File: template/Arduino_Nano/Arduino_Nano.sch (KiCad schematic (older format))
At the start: 6 parts, among them P1 Digital, P2 Analog, P3 CONN_1, P4 CONN_1, P5 CONN_1, P6 CONN_1

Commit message: add board Micro
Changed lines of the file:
@@
 L +3.3V #PWR3
 U 1 1 551D9E93
-P 11000 2575
-F 0 "#PWR3" H 11000 2535 30  0001 C CNN
-F 1 "+3.3V" H 11000 2685 30  0000 C CNN
-F 2 "" H 11000 2575 60  0000 C CNN
-F 3 "" H 11000 2575 60  0000 C CNN
-	1    11000 2575
+P 11125 2575
+F 0 "#PWR3" H 11125 2535 30  0001 C CNN
+F 1 "+3.3V" H 11125 2685 30  0000 C CNN
+F 2 "" H 11125 2575 60  0000 C CNN
+F 3 "" H 11125 2575 60  0000 C CNN
+	1    11125 2575
 	1    0    0    -1
 $EndComp
@@
 L +5V #PWR2
 U 1 1 551D9FBD
-P 11000 1575
-F 0 "#PWR2" H 11000 1665 20  0001 C CNN
-F 1 "+5V" H 11000 1665 30  0000 C CNN
-F 2 "" H 11000 1575 60  0000 C CNN
-F 3 "" H 11000 1575 60  0000 C CNN
-	1    11000 1575
+P 11125 1575
+F 0 "#PWR2" H 11125 1665 20  0001 C CNN
+F 1 "+5V" H 11125 1665 30  0000 C CNN
+F 2 "" H 11125 1575 60  0000 C CNN
+F 3 "" H 11125 1575 60  0000 C CNN
+	1    11125 1575
 	1    0    0    -1
 $EndComp
@@
 L GND #PWR4
 U 1 1 551D9FD7
-P 11125 1475
-F 0 "#PWR4" H 11125 1475 30  0001 C CNN
-F 1 "GND" H 11125 1405 30  0001 C CNN
-F 2 "" H 11125 1475 60  0000 C CNN
-F 3 "" H 11125 1475 60  0000 C CNN
-	1    11125 1475
+P 11000 1475
+F 0 "#PWR4" H 11000 1475 30  0001 C CNN
+F 1 "GND" H 11000 1405 30  0001 C CNN
+F 2 "" H 11000 1475 60  0000 C CNN
+F 3 "" H 11000 1475 60  0000 C CNN
+	1    11000 1475
 	1    0    0    -1
 $EndComp
@@
 	11225 2850 8600 2850
 Wire Wire Line
-	11000 1600 11000 1575
-Wire Wire Line
-	11125 1400 11125 1475
-Wire Wire Line
-	11000 2600 11000 2575
-Wire Wire Line
 	8750 1600 8750 1675
 Wire Wire Line
 	10500 2700 10875 2700
 Wire Wire Line
-	10500 2600 11000 2600
+	10500 2600 11125 2600
 Wire Wire Line
 	10500 2500 10875 2500
@@
 	10500 1700 10875 1700
 Wire Wire Line
-	10500 1600 11000 1600
+	10500 1600 11125 1600
 Wire Wire Line
 	10500 1500 10875 1500
-Wire Wire Line
-	10500 1400 11125 1400
 Wire Wire Line
 	10500 1300 10875 1300
@@
 Wire Wire Line
 	8875 1300 9425 1300
+Wire Wire Line
+	11125 1600 11125 1575
+Wire Wire Line
+	11000 1475 11000 1400
+Wire Wire Line
+	11000 1400 10500 1400
+Wire Wire Line
+	11125 2600 11125 2575
 $EndSCHEMATC

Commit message: Correction schématics
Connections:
- wire segments 34 -> 35
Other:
- moved on the sheet: P1, P2, P3, P4, P5, P6

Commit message: rebuilt shematic and fix librairie
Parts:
- removed P1: Digital, Socket_Arduino_Nano:Socket_Strip_Arduino_1x15, symbol CONN_15
- removed P2: Analog, Socket_Arduino_Nano:Socket_Strip_Arduino_1x15, symbol CONN_15
- removed P3, P4, P5, P6: CONN_1, Socket_Arduino_Nano:1pin_Nano, symbol CONN_1
- added P1: Digital, Socket_Arduino_Nano:Socket_Strip_Arduino_1x15, symbol CONN_01X15
- added P2: Analog, Socket_Arduino_Nano:Socket_Strip_Arduino_1x15, symbol CONN_01X15
- added P3, P4, P5, P6: CONN_01X01, Socket_Arduino_Nano:1pin_Nano, symbol CONN_01X01
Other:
- note added: "1"

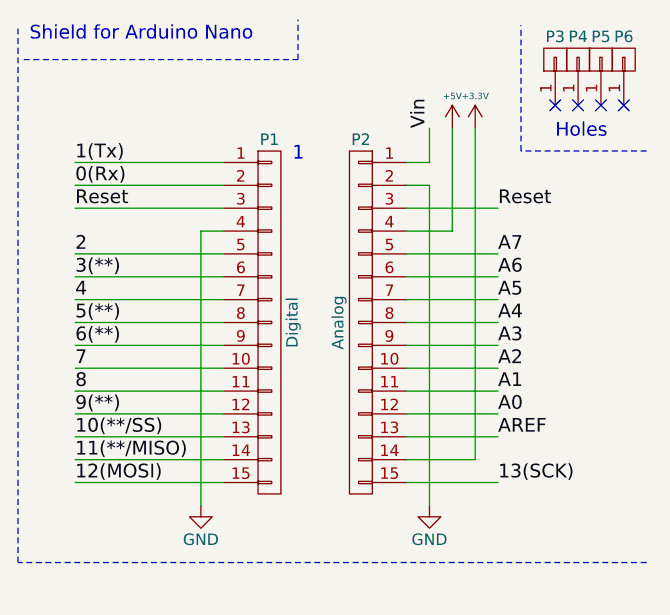
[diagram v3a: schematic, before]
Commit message: Fix pin order SS, MOSI, MISO, SCK
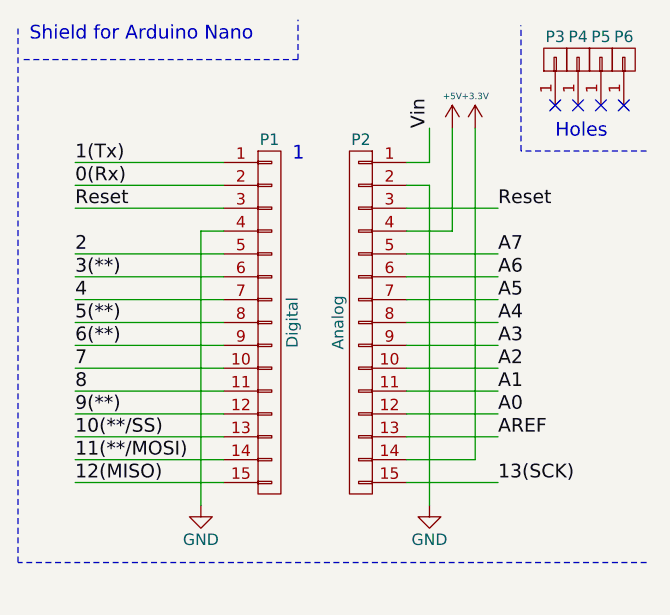
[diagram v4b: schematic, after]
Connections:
- net 11(**/MISO) renamed 11(**/MOSI)
- net 12(MOSI) renamed 12(MISO)
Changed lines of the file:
@@
 EESchema Schematic File Version 2
-LIBS:Arduino_Nano-rescue
 LIBS:power
 LIBS:device
@@
 10(**/SS)
 Text Label 8700 2400 0    60   ~ 0
-11(**/MISO)
+11(**/MOSI)
 Text Label 8700 2500 0    60   ~ 0
-12(MOSI)
+12(MISO)
 Text Label 10550 2500 0    60   ~ 0
 13(SCK)
